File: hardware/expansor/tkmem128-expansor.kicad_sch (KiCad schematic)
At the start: 4 parts, among them J1 Barramento TK, J2 Passagem, J3 Para a placa principal

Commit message: Esquematicos e silk rearranjados; pendencia do plano do soquete de borda
Esquematico das duas placas redesenhado a mao (havia simbolos saindo da
folha e sinais misturados) e serigrafia reorganizada. Conferido: ERC 0,
DRC 0, e a netlist exportada bate no a no com a intencao de projeto nas
duas placas (74 e 53 nets, zero divergencia).

Os geradores em tools/ passam a ser ferramenta de bootstrap: gen_schematic.py
e gen_pcb.py sobrescreveriam o ajuste manual. A fonte corrente e o conteudo
de hardware/. Documentado no README de tools/.

Registrada uma pendencia real da placa expansora (item 1b de
docs/ANTES-DE-FABRICAR.md): nas placas originais a fenda do soquete que
recebe os dedos do TK fica NO PLANO da placa, alinhada com os dedos de
passagem. O footprint atual e uma grade 2x28 de furos comuns, ou seja, o
conector monta por cima e a fenda fica alguns milimetros acima do plano —
o que joga a expansora abaixo do plano do TK e faz o periferico seguinte da
corrente descer outro tanto. Falta medir o conector para decidir entre
straddle mount e montagem por baixo.

Saidas de fabricacao e renders regerados a partir dos arquivos revisados.

Co-Authored-By: Claude Opus 5 <noreply@anthropic.com>
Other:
- moved on the sheet: C1, J1, J2, J3

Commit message: Arquitetura corrigida: conector na placa principal, tira soldada nos terminais
As fotos do periferico de audio (mesma construcao da TKMEM) mostraram como o
conjunto realmente se monta, e o datasheet do TE 5645235 confirmou o porque:

  - o conector de borda e de ENTRADA VERTICAL, ou seja, o cartao entra
    perpendicular a placa que o segura. Por isso ele vai soldado direto na
    placa PRINCIPAL, que fica em pe: a fenda cai no plano horizontal e recebe
    o cartao do TK;
  - os terminais atravessam a placa principal e sobram 3,18 mm do outro lado;
  - a tira de expansao encosta nesses terminais e e soldada neles. Ela nao tem
    conector nenhum: 56 ilhas de solda de um lado, dedos de borda do outro.

Com isso a tira fica coplanar com o cartao do TK e com a fenda do conector, e
a corrente de perifericos nao ganha degrau nenhum - que era o ponto levantado
na revisao.

Mudancas:

  placa principal  J1 troca do header 2x28 para o footprint do conector de
                   borda (2,54 x 4,85 mm, furo 1,02). O esquematico NAO mudou
                   (mesmo simbolo, mesmas nets), entao o rearranjo manual foi
                   preservado; so o cobre foi refeito.
  tira de expansao redesenhada: J1 = ilhas de solda 2x28, J2 = dedos de borda,
                   C1 de desacoplamento. 45 mm de comprimento.
  footprints       soquete passa a ter as 56 posicoes (a guia 5/52 e um
                   pedacinho de PCB que o montador encaixa, o conector tem
                   contato em todas). Novo ZX_TK_Bus_SolderPads_56.

Documentada tambem a orientacao de montagem: o lado dos componentes da placa
principal fica virado para a tira de expansao, nunca para o conector - ao
contrario a placa esbarra no micro dentro da caixa.

ERC 0, DRC 0 e netlist conferida no a no nas duas placas (74 e 53 nets).

Co-Authored-By: Claude Opus 5 <noreply@anthropic.com>
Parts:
- removed J1: Barramento TK, tkmem128:ZX_TK_Bus_Socket_56, symbol tkmem128:ZX_TK_Bus_56
- removed J3: Para a placa principal, tkmem128:ZX_TK_Bus_Header_2x28, symbol tkmem128:ZX_TK_Bus_Header_56
- added J1: Terminais do conector, tkmem128:ZX_TK_Bus_SolderPads_56, symbol tkmem128:ZX_TK_Bus_Header_56
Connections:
- net +5V: now also J1.3 (+5V (3))
- net A0: now also J1.9 (A0 (9))
- net A1: now also J1.10 (A1 (10))
- net A10: now also J1.30 (A10 (30))
- net A11: now also J1.28 (A11 (28))
- net A12: now also J1.2 (A12 (2))
- net A13: now also J1.55 (A13 (55))
- net A14: now also J1.1 (A14 (1))
- net A15: now also J1.56 (A15 (56))
- net A2: now also J1.11 (A2 (11))
- net A3: now also J1.12 (A3 (12))
- net A4: now also J1.24 (A4 (24))
- net A5: now also J1.23 (A5 (23))
- net A6: now also J1.22 (A6 (22))
- net A7: now also J1.21 (A7 (21))
- net A8: now also J1.31 (A8 (31))
- net A9: now also J1.27 (A9 (27))
- net BUS_9V: now also J1.4 (+9V (4))
- net BUS_BUSACK: now also J1.26 (BUSACK (26))
- net BUS_BUSREQ: now also J1.19 (BUSREQ (19))
- net BUS_CLK: now also J1.8 (CLOCK (8))
- net BUS_HALT: now also J1.42 (/HALT (42))
- net BUS_INT: now also J1.44 (/INT (44))
- net BUS_IORQGE: now also J1.13 (IORQGE (13))
- net BUS_M1: now also J1.33 (/M1 (33))
- net BUS_NMI: now also J1.43 (/NMI (43))
- net BUS_P07: now also J1.7 (NC/GND (7))
- net BUS_P15: now also J1.15 (GND/NC (15))
- net BUS_P16: now also J1.16 (NC (16))
- net BUS_P18: now also J1.18 (NC (18))
- net BUS_P29: now also J1.29 (NC (29))
- net BUS_P34: now also J1.34 (12V (34))
- net BUS_P35: now also J1.35 (12V (35))
- net BUS_P37: now also J1.37 (+5V/-5V (37))
- net BUS_RFSH: now also J1.32 (/RFSH (32))
- net BUS_SOUNDIN: now also J1.53 (SOUND IN (53))
- net BUS_WAIT: now also J1.36 (/WAIT (36))
- net D0: now also J1.51 (D0 (51))
- net D1: now also J1.50 (D1 (50))
- net D2: now also J1.49 (D2 (49))
- net D3: now also J1.46 (D3 (46))
- net D4: now also J1.45 (D4 (45))
- net D5: now also J1.47 (D5 (47))
- net D6: now also J1.48 (D6 (48))
- net D7: now also J1.54 (D7 (54))
- net GND: now also J1.14 (GND (14)), J1.5 (GND (5)), J1.52 (GND (52)), J1.6 (GND (6))
- net IORQ_N: now also J1.40 (/IORQ (40))
- net MREQ_N: now also J1.41 (/MREQ (41))
- net RAMDIS: now also J1.17 (RAMDIS (17))
- net RD_N: now also J1.39 (/RD (39))
- net RESET_N: now also J1.20 (/RESET (20))
- net ROMCS_BUS: now also J1.25 (ROMCS (25))
- net WR_N: now also J1.38 (/WR (38))

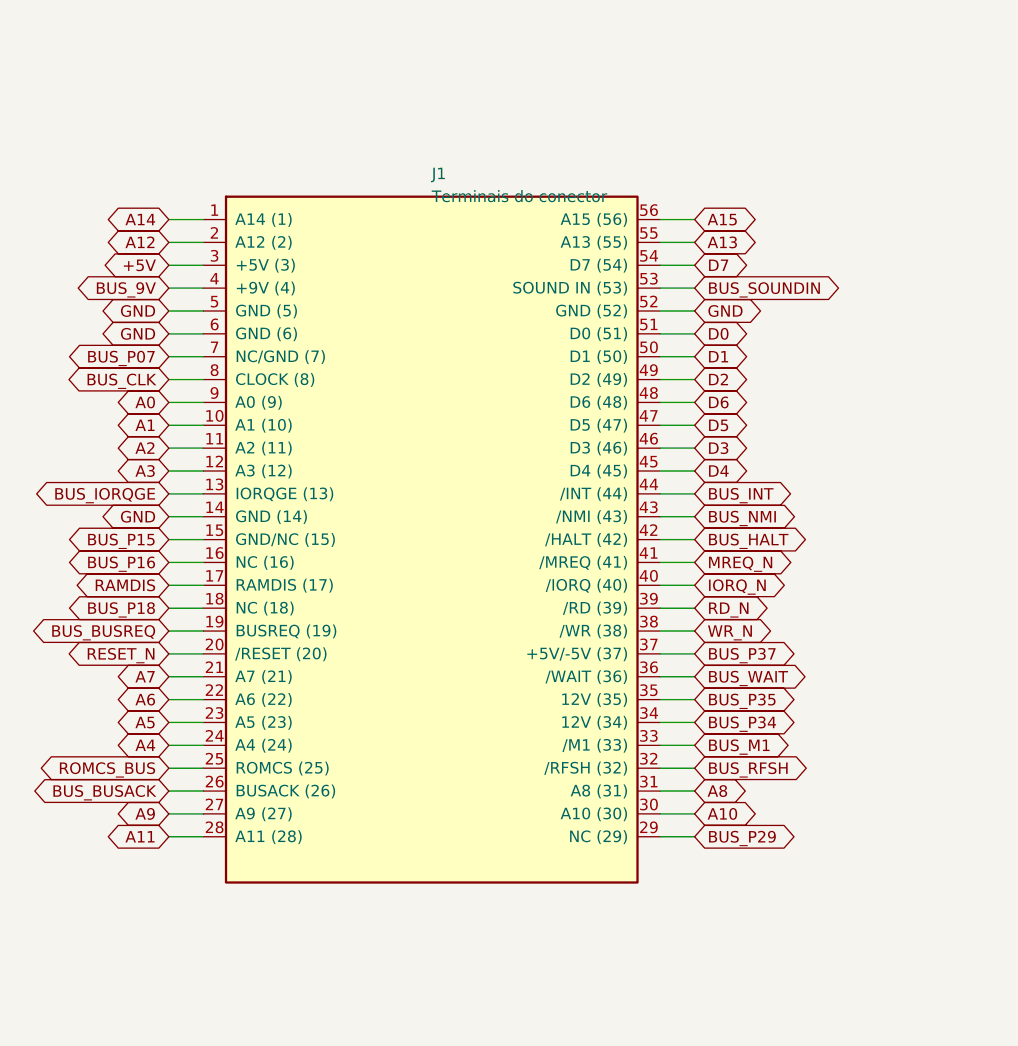
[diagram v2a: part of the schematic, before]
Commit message: Conector no verso, sem furos na guia, tira soldada dos dois lados
Tres correcoes de revisao:

1. A guia ocupa a posicao das vias 5 e 52, entao nao ha terminal ali e a placa
   nao precisa de furo. Footprint do conector volta de 56 para 54 furos. O
   simbolo continua com 56 pinos, o que deixou o esquematico rearranjado a mao
   intacto - o KiCad aceita os dois pinos sem ilha e o DRC fica zerado (sao
   GND, que tem ilha de sobra).

2. A placa principal estava invertida em relacao ao conector. Ele e o UNICO
   componente do lado do cobre: entra por baixo e e soldado por cima, pelo lado
   dos componentes, que fica virado para a tira de expansao. J1 passa para a
   camada B.Cu. O espelhamento que vem junto e a consequencia fisica de enfiar
   a peca pelo outro lado, e reforca o teste de continuidade do item 2.

3. A tira nao encosta nos terminais por fora: os terminais sao RETOS e ficam em
   duas fileiras a 4,85 mm, entao a tira entra ENTRE elas - uma fileira por
   cima, outra por baixo - e e soldada dos DOIS LADOS. O footprint passa a ter
   ilhas nas duas faces (F.Cu = 29..56, B.Cu = 1..28), nao SMD de uma face so.

Roteamento refeito nas duas placas, ambas 100% fechadas em 2 camadas com
isolacao de 0,14 mm. ERC 0, DRC 0 erros, 0 desconexoes, netlist conferida no a
no (74 e 53 nets). A serigrafia ajustada a mao foi preservada.

Co-Authored-By: Claude Opus 5 <noreply@anthropic.com>
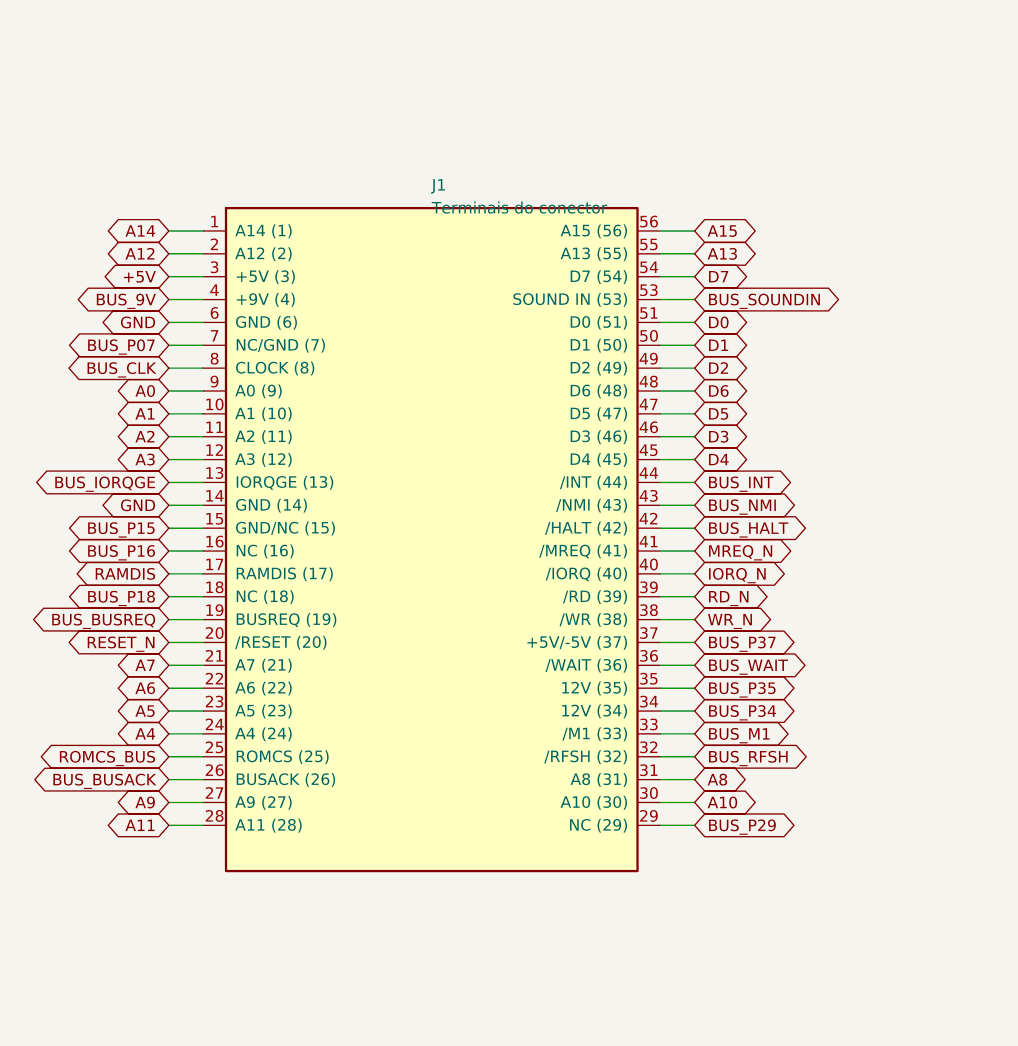
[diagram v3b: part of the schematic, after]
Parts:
- removed J1: Terminais do conector, tkmem128:ZX_TK_Bus_SolderPads_56, symbol tkmem128:ZX_TK_Bus_Header_56
- added J1: Terminais do conector, tkmem128:ZX_TK_Bus_SolderPads_56, symbol tkmem128:ZX_TK_Bus_56
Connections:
- net +5V: now also J1.3 (+5V (3))
- net A0: now also J1.9 (A0 (9))
- net A1: now also J1.10 (A1 (10))
- net A10: now also J1.30 (A10 (30))
- net A11: now also J1.28 (A11 (28))
- net A12: now also J1.2 (A12 (2))
- net A13: now also J1.55 (A13 (55))
- net A14: now also J1.1 (A14 (1))
- net A15: now also J1.56 (A15 (56))
- net A2: now also J1.11 (A2 (11))
- net A3: now also J1.12 (A3 (12))
- net A4: now also J1.24 (A4 (24))
- net A5: now also J1.23 (A5 (23))
- net A6: now also J1.22 (A6 (22))
- net A7: now also J1.21 (A7 (21))
- net A8: now also J1.31 (A8 (31))
- net A9: now also J1.27 (A9 (27))
- net BUS_9V: now also J1.4 (+9V (4))
- net BUS_BUSACK: now also J1.26 (BUSACK (26))
- net BUS_BUSREQ: now also J1.19 (BUSREQ (19))
- net BUS_CLK: now also J1.8 (CLOCK (8))
- net BUS_HALT: now also J1.42 (/HALT (42))
- net BUS_INT: now also J1.44 (/INT (44))
- net BUS_IORQGE: now also J1.13 (IORQGE (13))
- net BUS_M1: now also J1.33 (/M1 (33))
- net BUS_NMI: now also J1.43 (/NMI (43))
- net BUS_P07: now also J1.7 (NC/GND (7))
- net BUS_P15: now also J1.15 (GND/NC (15))
- net BUS_P16: now also J1.16 (NC (16))
- net BUS_P18: now also J1.18 (NC (18))
- net BUS_P29: now also J1.29 (NC (29))
- net BUS_P34: now also J1.34 (12V (34))
- net BUS_P35: now also J1.35 (12V (35))
- net BUS_P37: now also J1.37 (+5V/-5V (37))
- net BUS_RFSH: now also J1.32 (/RFSH (32))
- net BUS_SOUNDIN: now also J1.53 (SOUND IN (53))
- net BUS_WAIT: now also J1.36 (/WAIT (36))
- net D0: now also J1.51 (D0 (51))
- net D1: now also J1.50 (D1 (50))
- net D2: now also J1.49 (D2 (49))
- net D3: now also J1.46 (D3 (46))
- net D4: now also J1.45 (D4 (45))
- net D5: now also J1.47 (D5 (47))
- net D6: now also J1.48 (D6 (48))
- net D7: now also J1.54 (D7 (54))
- net GND: now also J1.14 (GND (14)), J1.6 (GND (6))
- net IORQ_N: now also J1.40 (/IORQ (40))
- net MREQ_N: now also J1.41 (/MREQ (41))
- net RAMDIS: now also J1.17 (RAMDIS (17))
- net RD_N: now also J1.39 (/RD (39))
- net RESET_N: now also J1.20 (/RESET (20))
- net ROMCS_BUS: now also J1.25 (ROMCS (25))
- net WR_N: now also J1.38 (/WR (38))

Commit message: Serigrafia da tira: numeracao por face, nas duas faces
As ilhas de J1 e os dedos de J2 sao SMD — cada pino existe em UMA face so. Na
coluna x=73,66 o cobre de F.Cu e o pino 56 e o de B.Cu e o pino 1. A serigrafia
da frente de J1 estava escrita "1" e "28": nomeando os pads de tras. Vira
56 / 29. J2, do lado, ja estava certo, o que so deixava a divergencia mais
visivel na placa.

A tira e soldada dos DOIS lados, entao quem monta olha as duas faces. Cada face
passa a trazer a numeracao dos seus proprios pinos, em J1 e em J2:

  F.Silkscreen   29 ..... 56      (os pads de F.Cu)
  B.Silkscreen    1 ..... 28      (os pads de B.Cu)

Vem trocado de lado entre as faces porque e a mesma placa vista por tras.
"SOLDAR DOS DOIS LADOS" tambem passa a aparecer no verso, que e justamente onde
alguem pode nao perceber que ha o que soldar.

Contorno de J1 refeito: era um retangulo fechado, mas do lado das ilhas fica a
ARESTA da placa, entao um dos lados caia fora da placa e a marca da guia
atravessava a borda (3 avisos de silk_edge_clearance, agora duplicados ao levar
o desenho para o verso). Vira um U aberto para a aresta, parando 0,3 mm antes
dela, nas duas faces. DRC da tira: de 3 avisos para 0.

"PASSAGEM ->" era ambiguo: a flecha apontava para +x, mas os dedos ficam para
baixo. Vira "PARA OUTROS PERIFERICOS", centrado logo acima deles — a
proximidade ja diz a direcao, e o texto diz o que e.

confere_alinhamento.py ganhou a verificacao dessa classe de erro: para cada
rotulo numerico de serigrafia, acha o pad mais proximo NAQUELA face e exige que
o numero bata. Verificado com teste negativo (reintroduzir o erro faz o script
sair com codigo 1). Vale para as duas placas.

Inclui o rearranjo manual do Leonardo no esquematico e na serigrafia das duas
placas.

DRC 0 violacoes, 0 desconexoes. Alinhamento entre as placas inalterado.

Co-Authored-By: Claude Opus 5 <noreply@anthropic.com>
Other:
- moved on the sheet: C1

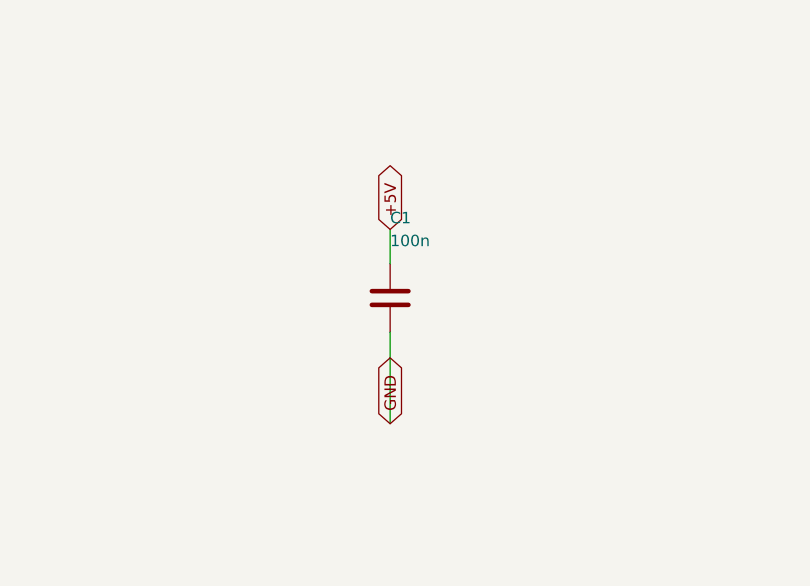
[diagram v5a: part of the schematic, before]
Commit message: Tira: 54 retas de 1,5 mm, zero via, zero plano de terra
Voce esta certo nas tres criticas. Medindo o que estava la:

  trilha de sinal      0,25 mm
  cobre por face       B.Cu 1885 mm  x  F.Cu 423 mm   (82% numa face so)
  vias                 53

Numa placa que alimenta uma cascata de perifericos isso e indefensavel. E o pior
e que a tira nem tem problema de roteamento: J1 e J2 estao nas MESMAS colunas e
cada pino fica na MESMA face nos dois (F.Cu = 29..56, B.Cu = 1..28). Cada rede e
uma reta vertical de x constante. Nao existe um unico cruzamento na placa. O
Freerouting nao sabia disso e inventou 53 vias.

Refeito a mao, sem autorouter:

  54 trilhas retas de 1,5 mm
  0 vias
  F.Cu 1044,6 mm  x  B.Cu 1044,6 mm   (simetrico ao milimetro)

1,5 mm e a largura maxima limpa: os dedos de J2 tem 1,524 mm e o passo e 2,54,
sobrando 1,04 mm de vao entre vizinhas. Suporta ~3,5 A contra ~0,9 A antes.

Plano de terra removido, como voce pediu. Com as verticais ocupando as duas
faces inteiras, o plano so existia em fiapos de 1 mm entre trilhas — inutil como
retorno, util so para criar acoplamento.

C1 SAIU, e por um motivo estrutural que vale registrar: numa placa de passagem
com ilhas presas a uma face, cada COLUNA carrega redes diferentes nas duas
faces. Em x=68,58, B.Cu e +5V e F.Cu e D7. Entao QUALQUER ilha passante fora da
coluna da guia e um curto entre duas redes. C1 era THT. E nem em SMD caberia:
BUS_9V (x=66,04) fica entre o +5V (68,58) e o GND mais proximo (60,96), com as
duas faces ocupadas — nao ha caminho de 2 camadas de um ao outro. O
desacoplamento fica na principal (5x100n + 10u) e no periferico seguinte.

Entrou W1, o link de terra: os pinos 6 e 14 sao os dois GND do barramento, e
liga-los exigiria cruzar 7 colunas. Duas ilhas SMD em B.Cu e um fio isolado por
cima resolvem — e e o retorno de terra de tudo que vier em cascata. Footprint
board_only: fio e ligacao de cobre, nao componente, entao nao tem simbolo nem
entra na lista de material.

DRC 0 violacoes. O 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
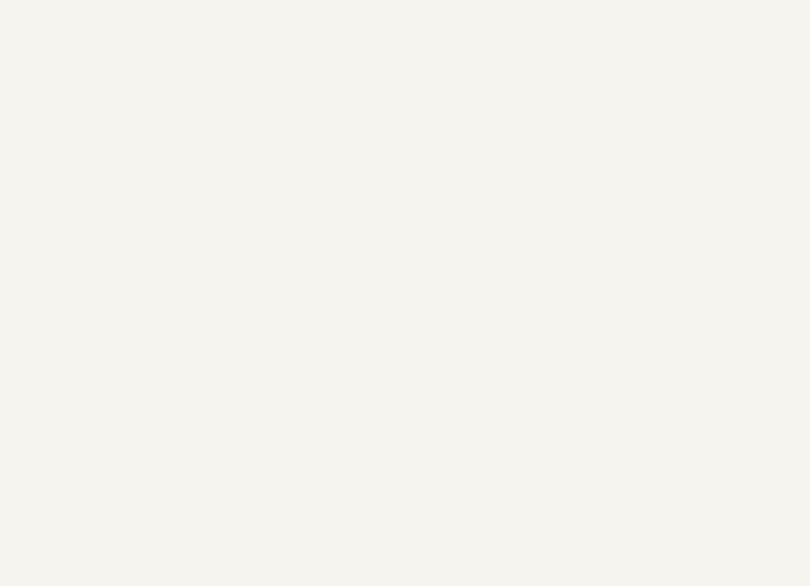
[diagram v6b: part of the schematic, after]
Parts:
- removed C1: 100n, Capacitor_THT:C_Disc_D5.0mm_W2.5mm_P5.00mm, symbol Device:C
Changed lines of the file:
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@@
 	(wire
 		(pts
-			(xy 377.19 193.04) (xy 377.19 203.2)
-		)
-		(stroke
-			(width 0)
-			(type default)
-		)
-	)
-	(wire
-		(pts
 			(xy 44.45 189.23) (xy 40.64 189.23)
 		)
@@
 	(wire
 		(pts
-			(xy 377.19 185.42) (xy 377.19 181.61)
-		)
-		(stroke
-			(width 0)
-			(type default)
-		)
-	)
-	(wire
-		(pts
 			(xy 275.59 156.21) (xy 279.4 156.21)
 		)
@@
 		)
 	)
-	(global_label "GND"
-		(shape bidirectional)
-		(at 377.19 203.2 90)
-		(fields_autoplaced yes)
-		(effects
-			(font
-				(size 1.27 1.27)
-			)
-			(justify left)
-		)
-		(property "Intersheetrefs" "${INTERSHEET_REFS}"
-			(at 377.19 203.2 0)
-			(hide yes)
-			(show_name no)
-			(do_not_autoplace no)
-			(effects
-				(font
-					(size 1.27 1.27)
-				)
-			)
-		)
-	)
 	(global_label "BUS_M1"
 		(shape bidirectional)
@@
 		)
 	)
-	(global_label "+5V"
-		(shape bidirectional)
-		(at 377.19 181.61 90)
-		(fields_autoplaced yes)
-		(effects
-			(font
-				(size 1.27 1.27)
-			)
-			(justify left)
-		)
-		(property "Intersheetrefs" "${INTERSHEET_REFS}"
-			(at 377.19 181.61 0)
-			(hide yes)
-			(show_name no)
-			(do_not_autoplace no)
-			(effects
-				(font
-					(size 1.27 1.27)
-				)
-			)
-		)
-	)
 	(global_label "D5"
 		(shape bidirectional)
@@
 					(unit 1)
 				)
-			)
-		)
-	)
-	(symbol
-		(lib_id "Device:C")
-		(at 377.19 189.23 0)
-		(unit 1)
-		(body_style 1)
-		(exclude_from_sim no)
-		(in_bom yes)
-		(on_board yes)
-		(in_pos_files yes)
-		(dnp no)
-		(property "Reference" "C1"
-			(at 377.19 180.34 0)
-			(show_name no)
-			(do_not_autoplace no)
-			(effects
-				(font
-					(size 1.27 1.27)
-				)
-				(justify left)
-			)
-		)
-		(property "Value" "100n"
-			(at 377.19 182.88 0)
-			(show_name no)
-			(do_not_autoplace no)
-			(effects
-				(font
-					(size 1.27 1.27)
-				)
-				(justify left)
-			)
-		)
-		(property "Footprint" "Capacitor_THT:C_Disc_D5.0mm_W2.5mm_P5.00mm"
-			(at 377.19 189.23 0)
-			(hide yes)
-			(show_name no)
-			(do_not_autoplace no)
-			(effects
-				(font
-					(size 1.27 1.27)
-				)
-			)
-		)
-		(property "Datasheet" ""
-			(at 377.19 189.23 0)
-			(hide yes)
-			(show_name no)
-			(do_not_autoplace no)
-			(effects
-				(font
-					(size 1.27 1.27)
-				)
-			)
-		)
-		(property "Description" "Desacoplamento junto ao ponto de alimentacao"
-			(at 377.19 189.23 0)
-			(hide yes)
-			(show_name no)
-			(do_not_autoplace no)
-			(effects
-				(font
-					(size 1.27 1.27)
-				)
-			)
-		)
-		(pin "1"
-		)
-		(pin "2"
-		)
-		(instances
-			(project "tkmem128-expansor"
-				(path "/8c22154b-c952-396c-6e1c-0ae032eedbbc"
-					(reference "C1")
-					(unit 1)
-				)
